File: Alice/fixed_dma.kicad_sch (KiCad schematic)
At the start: 122 parts, among them Q285 NOT_OC, Q286 NOT_OC, Q287 NOT_OC, Q288 NOT_OC, Q289 NOT_OC, Q290 NOT_OC, Q291 NOT_OC, Q292 NOT_OC, Q293 NOT_OC, Q294 NOT_OC, Q295 NOT_OC, Q296 NOT_OC, Q297 NOT_OC, Q298 NOT_OC, Q299 NOT_OC, Q300 NOT_OC, Q301 NOT_OC, Q302 NOT_OC, Q303 NOT_OC, Q304 NOT_OC, Q305 NOT_OC, Q306 NOT_OC, Q307 NOT_OC, Q308 NOT_OC, Q309 NOT_OC, Q310 NOT_OC, Q311 NOT_OC, Q312 NOT_OC, Q313 NOT_OC, Q314 NOT_OC, Q315 NOT_OC, Q316 NOT_OC, Q317 NOT_OC, Q318 NOT_OC, Q319 NOT_OC, Q320 NOT_OC, Q321 NOT_OC, Q322 NOT_OC, Q323 NOT_OC, Q324 NOT_OC, Q325 NOT_OC, Q326 NOT_OC, Q327 NOT_OC, Q328 NOT_OC, Q329 NOT_OC, Q330 NOT_OC, Q331 NOT_OC, Q332 NOT_OC

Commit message: RGA bus added (WIP), I/Os renamed with PAD_ prefix
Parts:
- added AND_47, AND_48: AND3, symbol NMOS:AND3
- added DBR_Q1: PASS, symbol NMOS:PASS
- added NOT_19, NOT_20, NOT_21: NOT, symbol NMOS:NOT
- added RGA_INB1, RGA_INB2, RGA_INB3, RGA_INB4, RGA_INB5, RGA_INB6, RGA_INB7, RGA_INB8: FAINB, symbol NMOS:FAINB
- added RGA_MUX1, RGA_MUX2, RGA_MUX3, RGA_MUX4, RGA_MUX5, RGA_MUX6, RGA_MUX7, RGA_MUX8: FAMUX, symbol NMOS:FAMUX
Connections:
- net CCKF: now also DBR_Q1.2 (G)
- net CCKR: now also AND_47.3, AND_48.3
- net DBR: now also AND_47.2, AND_48.2, NOT_20.1, NOT_21.2; no longer DBR_FF1.1 (Q)
- net DDRB1: now also RGA_MUX1.3 (B)
- net DDRB2: now also RGA_MUX2.3 (B)
- net DDRB3: now also RGA_MUX3.3 (B)
- net DDRB4: now also RGA_MUX4.3 (B)
- net DDRB5: now also RGA_MUX5.3 (B)
- net DDRB6: now also RGA_MUX6.3 (B)
- net DDRB7: now also RGA_MUX7.3 (B)
- net DDRB8: now also RGA_MUX8.3 (B)
- net EUAP: now also OR_27.5; no longer OR_27.2
- net EUCP: now also OR_27.2; no longer OR_27.5
- net EVEN: now also AND_43.2; no longer AND_43.3
- net HT4: now also AND_43.3; no longer AND_43.4
- net LOL: now also AND_43.4; no longer AND_43.2
- net PHI1: now also RGA_INB1.4 (CK), RGA_INB2.4 (CK), RGA_INB3.4 (CK), RGA_INB4.4 (CK), RGA_INB5.4 (CK), RGA_INB6.4 (CK), RGA_INB7.4 (CK), RGA_INB8.4 (CK)
- net UXPD: now also DBR_Q1.1 (D)
- net BLS renamed PAD_NBLS
- net DMAL renamed PAD_DMAL
- new net: AND_47.1, RGA_MUX1.5 (SA), RGA_MUX2.5 (SA), RGA_MUX3.5 (SA), RGA_MUX4.5 (SA), RGA_MUX5.5 (SA), RGA_MUX6.5 (SA), RGA_MUX7.5 (SA), RGA_MUX8.5 (SA)
- new net: AND_48.1, RGA_MUX1.6 (SB), RGA_MUX2.6 (SB), RGA_MUX3.6 (SB), RGA_MUX4.6 (SB), RGA_MUX5.6 (SB), RGA_MUX6.6 (SB), RGA_MUX7.6 (SB), RGA_MUX8.6 (SB)
- new net: RGA_MUX1.8 (FF), RGA_MUX2.8 (FF), RGA_MUX3.8 (FF), RGA_MUX4.8 (FF), RGA_MUX5.8 (FF), RGA_MUX6.8 (FF), RGA_MUX7.8 (FF), RGA_MUX8.8 (FF)
- new net: AND_48.4, NOT_19.1
- new net CIR1: RGA_MUX1.2 (A)
- new net CIR2: RGA_MUX2.2 (A)
- new net CIR3: RGA_MUX3.2 (A)
- new net CIR4: RGA_MUX4.2 (A)
- new net CIR5: RGA_MUX5.2 (A)
- new net CIR6: RGA_MUX6.2 (A)
- new net CIR7: RGA_MUX7.2 (A)
- new net CIR8: RGA_MUX8.2 (A)
- new net COPRS: AND_47.4, NOT_19.2
- new net DDBR: DBR_FF1.1 (Q)
- new net NDBR: DBR_Q1.3 (S), NOT_20.2, RGA_MUX1.7 (SC), RGA_MUX2.7 (SC), RGA_MUX3.7 (SC), RGA_MUX4.7 (SC), RGA_MUX5.7 (SC), RGA_MUX6.7 (SC), RGA_MUX7.7 (SC), RGA_MUX8.7 (SC)
- new net PAD_NDBR: NOT_21.1
- new net RGA1: RGA_INB1.3 (I), RGA_MUX1.1 (Q)
- new net RGA2: RGA_INB2.3 (I), RGA_MUX2.1 (Q)
- new net RGA3: RGA_INB3.3 (I), RGA_MUX3.1 (Q)
- new net RGA4: RGA_INB4.3 (I), RGA_MUX4.1 (Q)
- new net RGA5: RGA_INB5.3 (I), RGA_MUX5.1 (Q)
- new net RGA6: RGA_INB6.3 (I), RGA_MUX6.1 (Q)
- new net RGA7: RGA_INB7.3 (I), RGA_MUX7.1 (Q)
- new net RGA8: RGA_INB8.3 (I), RGA_MUX8.1 (Q)
- new net RGB1: RGA_INB1.1 (O)
- new net RGB2: RGA_INB2.1 (O)
- new net RGB3: RGA_INB3.1 (O)
- new net RGB4: RGA_INB4.1 (O)
- new net RGB5: RGA_INB5.1 (O)
- new net RGB6: RGA_INB6.1 (O)
- new net RGB7: RGA_INB7.1 (O)
- new net RGB8: RGA_INB8.1 (O)
- new net UPA1: RGA_MUX1.4 (C)
- new net UPA2: RGA_MUX2.4 (C)
- new net UPA3: RGA_MUX3.4 (C)
- new net UPA4: RGA_MUX4.4 (C)
- new net UPA5: RGA_MUX5.4 (C)
- new net UPA6: RGA_MUX6.4 (C)
- new net UPA7: RGA_MUX7.4 (C)
- new net UPA8: RGA_MUX8.4 (C)
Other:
- moved on the sheet: BLS_FF1, BSTREI_FF1, DMAL_FF1, DMAL_FF2, DMAL_FF3, DRB_FF1, DRB_FF2, DRB_FF3, DRB_FF4, DRB_FF5, DRB_FF6, DRB_FF7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

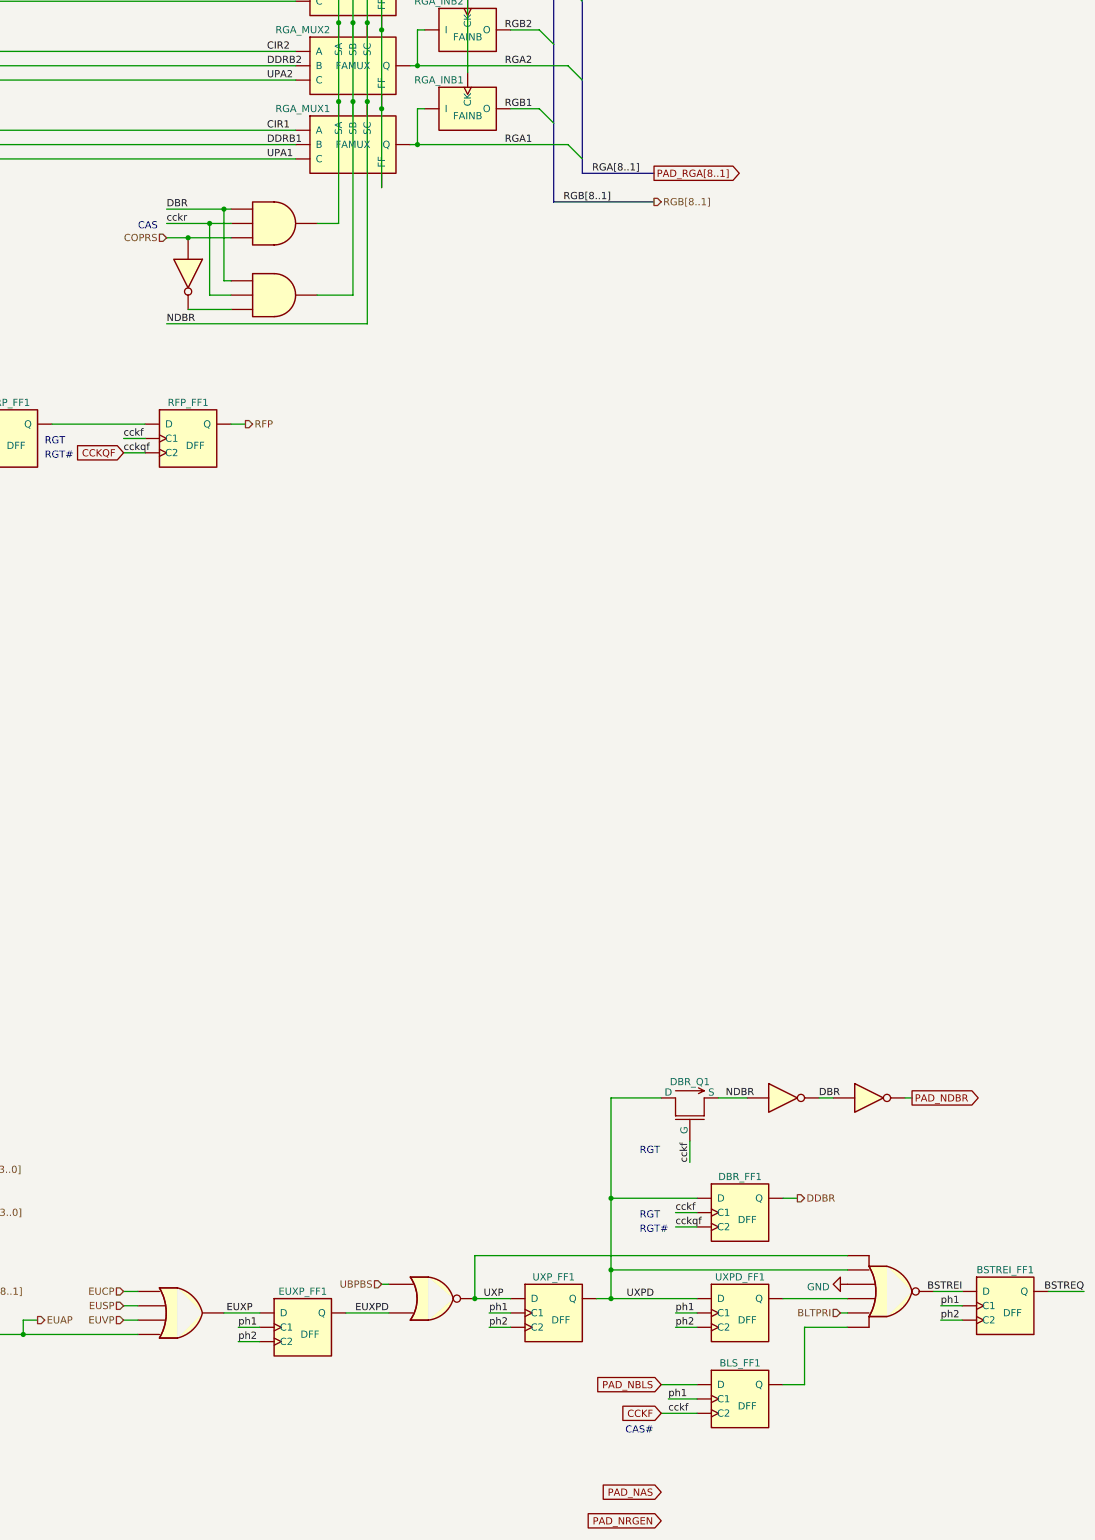
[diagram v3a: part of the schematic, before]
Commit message: Sheet RGA decode added
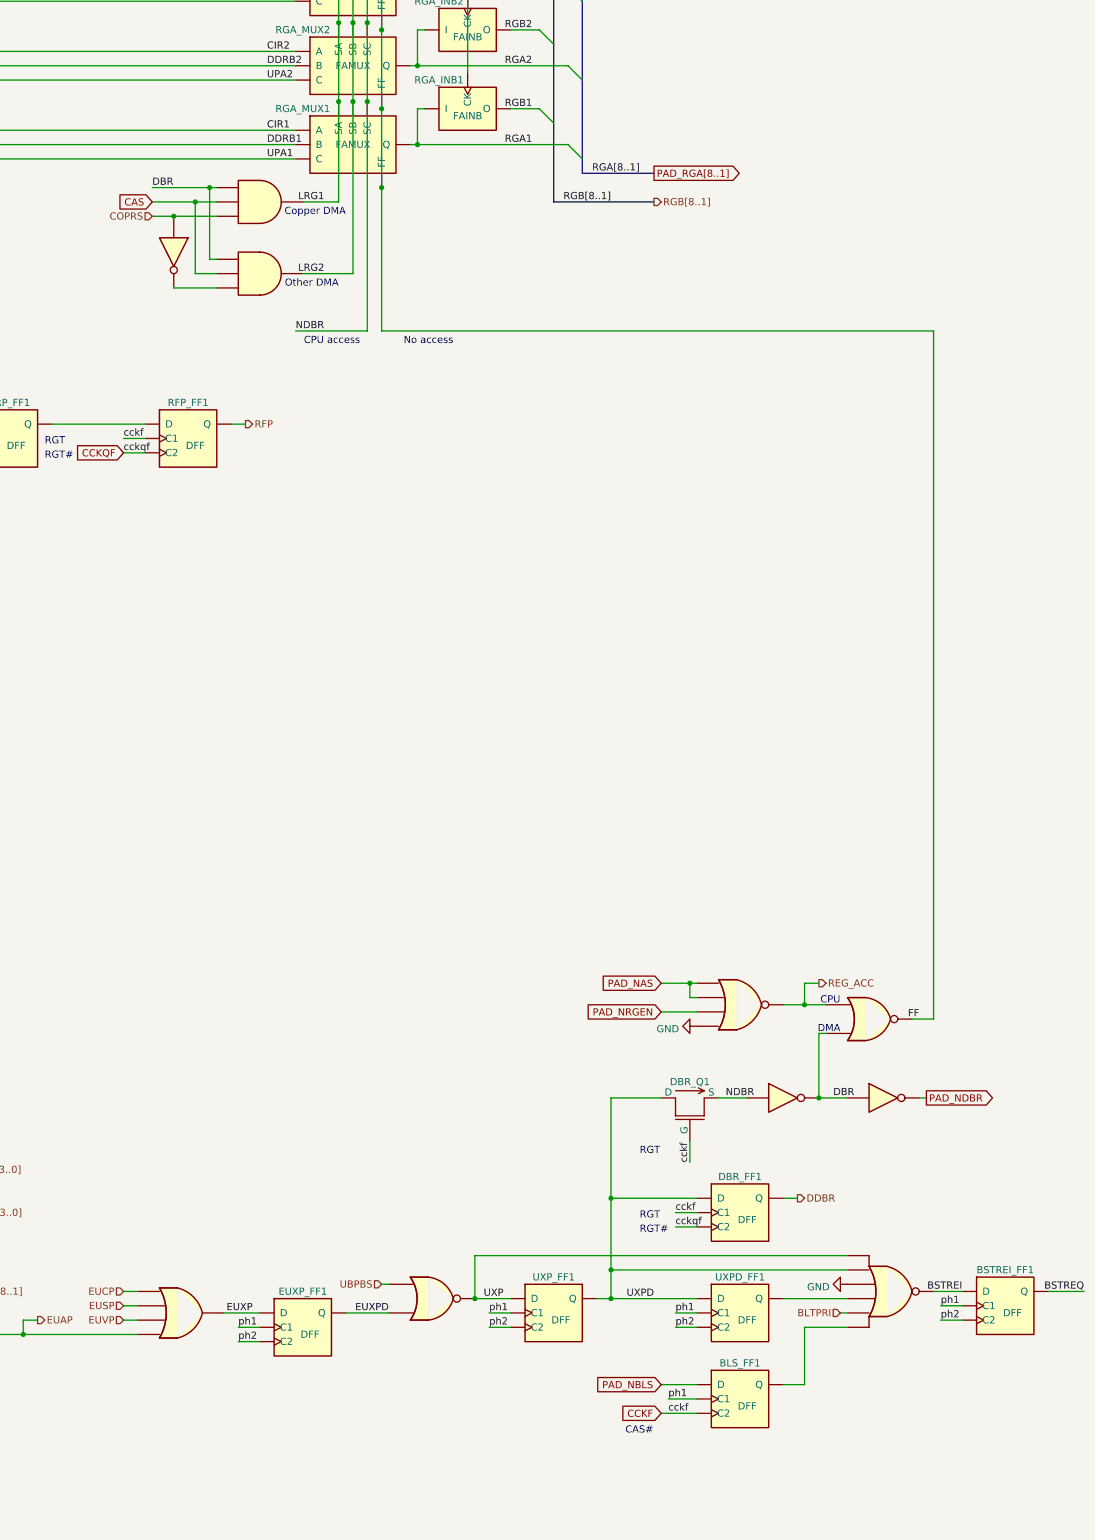
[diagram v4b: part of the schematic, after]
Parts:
- added NOR_21: NOR4, symbol NMOS:NOR4
- added NOR_22: NOR2, symbol NMOS:NOR2
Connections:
- net CCKR: no longer AND_47.3, AND_48.3
- net DBR: now also NOR_22.3
- net GND: now also NOR_21.5
- net PAD_NAS: now also NOR_21.2, NOR_21.3
- net PAD_NRGEN: now also NOR_21.4
- net LRG1: now reaches AND_47.1, RGA_MUX1.5 (SA), RGA_MUX2.5 (SA), RGA_MUX3.5 (SA), RGA_MUX4.5 (SA), RGA_MUX5.5 (SA), RGA_MUX6.5 (SA), RGA_MUX7.5 (SA), RGA_MUX8.5 (SA)
- net LRG2: now reaches AND_48.1, RGA_MUX1.6 (SB), RGA_MUX2.6 (SB), RGA_MUX3.6 (SB), RGA_MUX4.6 (SB), RGA_MUX5.6 (SB), RGA_MUX6.6 (SB), RGA_MUX7.6 (SB), RGA_MUX8.6 (SB)
- net FF: now reaches RGA_MUX1.8 (FF), RGA_MUX2.8 (FF), RGA_MUX3.8 (FF), RGA_MUX4.8 (FF), RGA_MUX5.8 (FF), RGA_MUX6.8 (FF), RGA_MUX7.8 (FF), RGA_MUX8.8 (FF)
- net FF: now also NOR_22.1
- new net CAS: AND_47.3, AND_48.3
- new net REG_ACC: NOR_21.1, NOR_22.2
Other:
- note added: "CPU"
- note added: "CPU access"
- note added: "Copper DMA"
- note added: "DMA"
- note added: "No access"
- note added: "Other DMA"

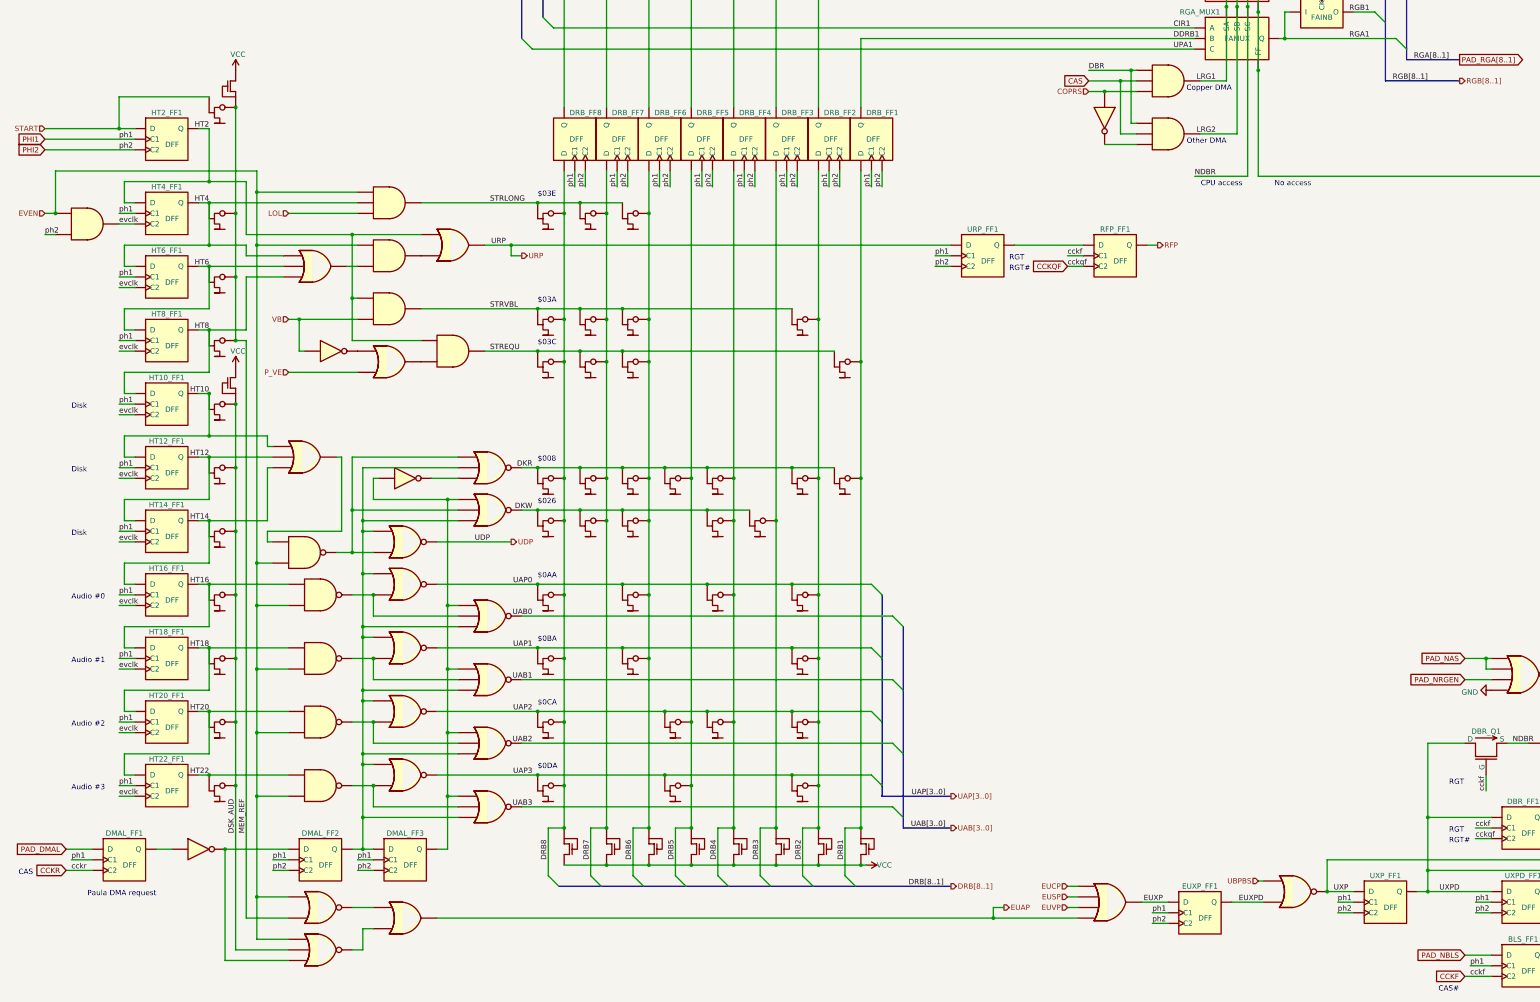
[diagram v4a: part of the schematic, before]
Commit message: Some refactoring : BEAMCON0 and BPLCON0 moved to the top sheet, CLOCKGEN added
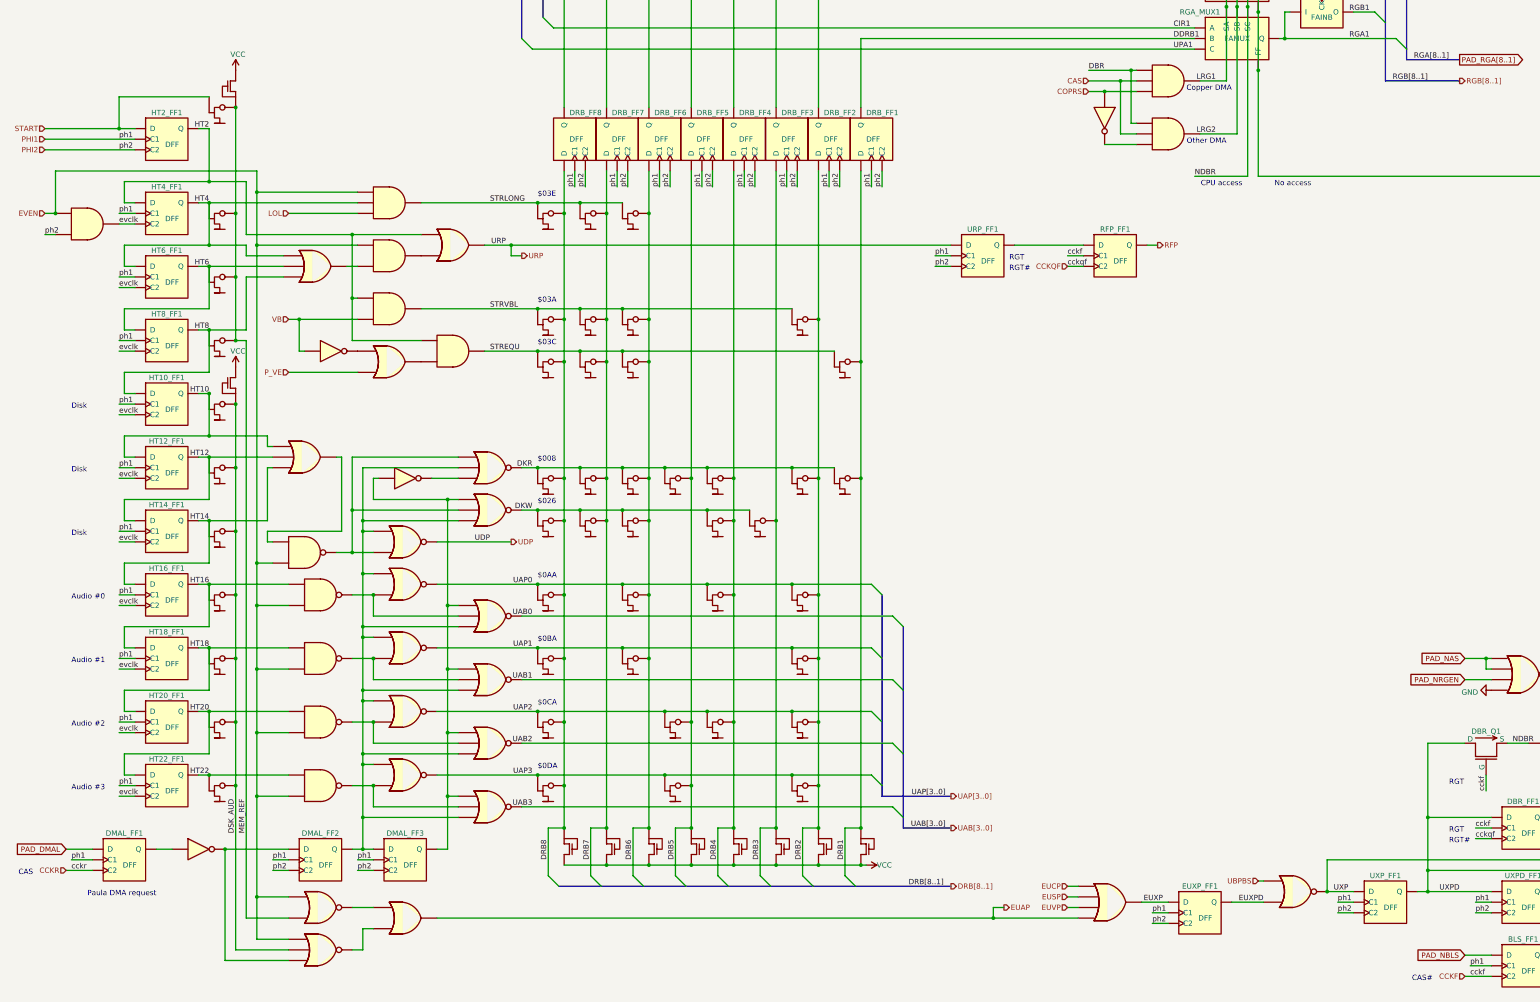
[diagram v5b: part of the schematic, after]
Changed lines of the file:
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@@
     (effects (font (size 1.27 1.27)) (justify left bottom))
   )
-  (text "CAS#" (at 373.38 358.14 0)
+  (text "CAS#" (at 367.03 355.6 0)
     (effects (font (size 1.27 1.27)) (justify left bottom))
   )
@@
     )
   )
-  (global_label "CAS" (shape input) (at 289.56 139.7 180) (fields_autoplaced)
-    (effects (font (size 1.27 1.27)) (justify right))
-    (property "Intersheet References" "${INTERSHEET_REFS}" (id 0) (at 283.5788 139.6206 0)
-      (effects (font (size 1.27 1.27)) (justify right) hide)
-    )
-  )
-  (global_label "CCKQF" (shape input) (at 284.48 184.15 180) (fields_autoplaced)
-    (effects (font (size 1.27 1.27)) (justify right))
-    (property "Intersheet References" "${INTERSHEET_REFS}" (id 0) (at 275.8379 184.0706 0)
-      (effects (font (size 1.27 1.27)) (justify right) hide)
-    )
-  )
-  (global_label "CCKR" (shape input) (at 44.45 328.93 180) (fields_autoplaced)
-    (effects (font (size 1.27 1.27)) (justify right))
-    (property "Intersheet References" "${INTERSHEET_REFS}" (id 0) (at 36.9569 328.8506 0)
-      (effects (font (size 1.27 1.27)) (justify right) hide)
-    )
-  )
-  (global_label "PHI2" (shape input) (at 39.37 156.21 180) (fields_autoplaced)
-    (effects (font (size 1.27 1.27)) (justify right))
-    (property "Intersheet References" "${INTERSHEET_REFS}" (id 0) (at 32.5421 156.1306 0)
-      (effects (font (size 1.27 1.27)) (justify right) hide)
-    )
-  )
   (global_label "PAD_NBLS" (shape input) (at 379.73 349.25 180) (fields_autoplaced)
     (effects (font (size 1.27 1.27)) (justify right))
@@
     )
   )
-  (global_label "CCKF" (shape input) (at 379.73 354.33 180) (fields_autoplaced)
-    (effects (font (size 1.27 1.27)) (justify right))
-    (property "Intersheet References" "${INTERSHEET_REFS}" (id 0) (at 372.4183 354.2506 0)
-      (effects (font (size 1.27 1.27)) (justify right) hide)
-    )
-  )
   (global_label "PAD_RGA[8..1]" (shape output) (at 378.46 134.62 0) (fields_autoplaced)
     (effects (font (size 1.27 1.27)) (justify left))
@@
     )
   )
-  (global_label "PHI1" (shape input) (at 39.37 153.67 180) (fields_autoplaced)
-    (effects (font (size 1.27 1.27)) (justify right))
-    (property "Intersheet References" "${INTERSHEET_REFS}" (id 0) (at 32.5421 153.5906 0)
-      (effects (font (size 1.27 1.27)) (justify right) hide)
-    )
-  )
   (global_label "PAD_NDBR" (shape output) (at 426.72 298.45 0) (fields_autoplaced)
     (effects (font (size 1.27 1.27)) (justify left))
@@
     (effects (font (size 1.27 1.27)) (justify left))
   )
+  (hierarchical_label "CAS" (shape input) (at 289.56 139.7 180)
+    (effects (font (size 1.27 1.27)) (justify right))
+  )
   (hierarchical_label "REG_ACC" (shape output) (at 407.67 278.13 0)
     (effects (font (size 1.27 1.27)) (justify left))
@@
     (effects (font (size 1.27 1.27)) (justify right))
   )
+  (hierarchical_label "PHI1" (shape input) (at 39.37 153.67 180)
+    (effects (font (size 1.27 1.27)) (justify right))
+  )
   (hierarchical_label "DDBR" (shape output) (at 403.86 316.23 0)
     (effects (font (size 1.27 1.27)) (justify left))
@@
     (effects (font (size 1.27 1.27)) (justify right))
   )
+  (hierarchical_label "CCKF" (shape input) (at 379.73 354.33 180)
+    (effects (font (size 1.27 1.27)) (justify right))
+  )
   (hierarchical_label "COPRS" (shape input) (at 289.56 142.24 180)
     (effects (font (size 1.27 1.27)) (justify right))
   )
+  (hierarchical_label "CCKQF" (shape input) (at 284.48 184.15 180)
+    (effects (font (size 1.27 1.27)) (justify right))
+  )
   (hierarchical_label "EUVP" (shape input) (at 284.48 337.82 180)
     (effects (font (size 1.27 1.27)) (justify right))
@@
     (effects (font (size 1.27 1.27)) (justify left))
   )
+  (hierarchical_label "PHI2" (shape input) (at 39.37 156.21 180)
+    (effects (font (size 1.27 1.27)) (justify right))
+  )
   (hierarchical_label "UAB[3..0]" (shape output) (at 256.54 318.77 0)
     (effects (font (size 1.27 1.27)) (justify left))
@@
     (effects (font (size 1.27 1.27)) (justify left))
   )
+  (hierarchical_label "CCKR" (shape input) (at 44.45 328.93 180)
+    (effects (font (size 1.27 1.27)) (justify right))
+  )
   (hierarchical_label "P_VE" (shape input) (at 97.79 209.55 180)
